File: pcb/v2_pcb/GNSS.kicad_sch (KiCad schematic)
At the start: 22 parts, among them J900 U.FL / Beitian BT-T076, U900 UM980

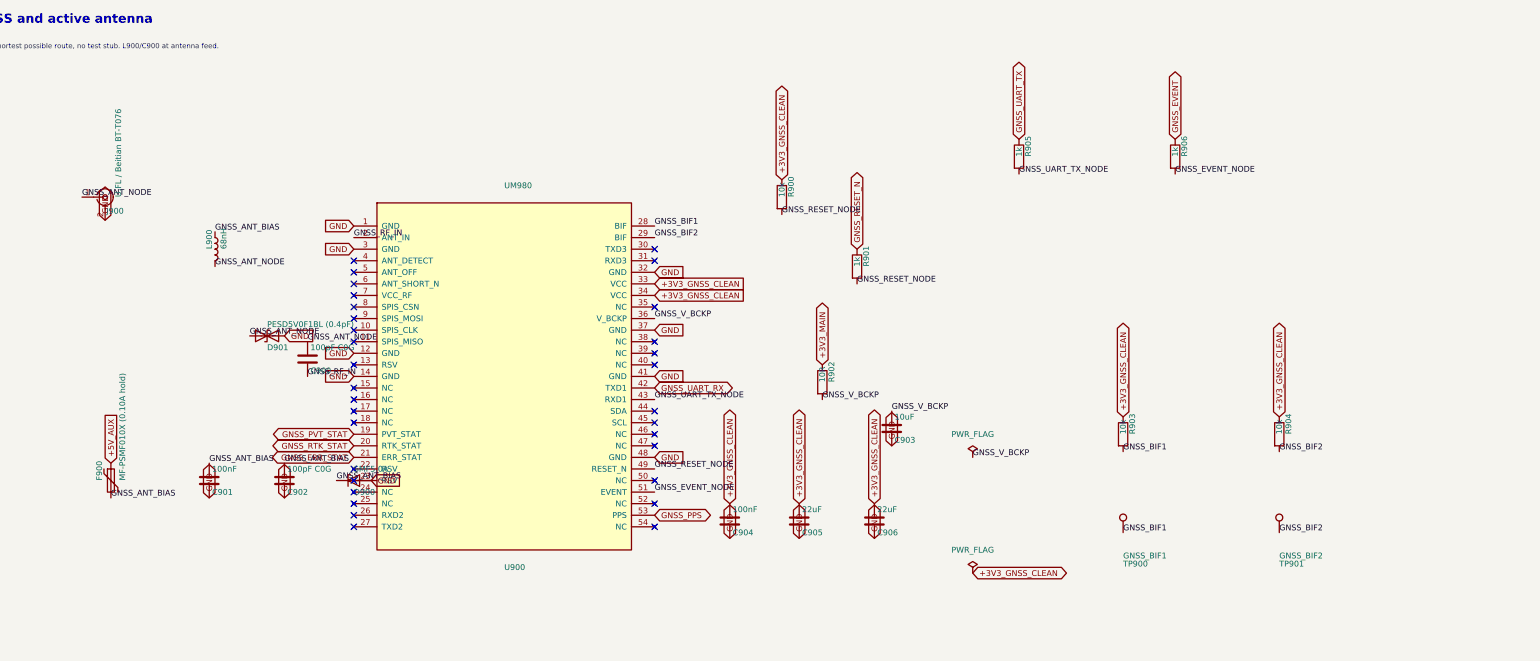
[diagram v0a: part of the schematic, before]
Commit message: switch mosfets
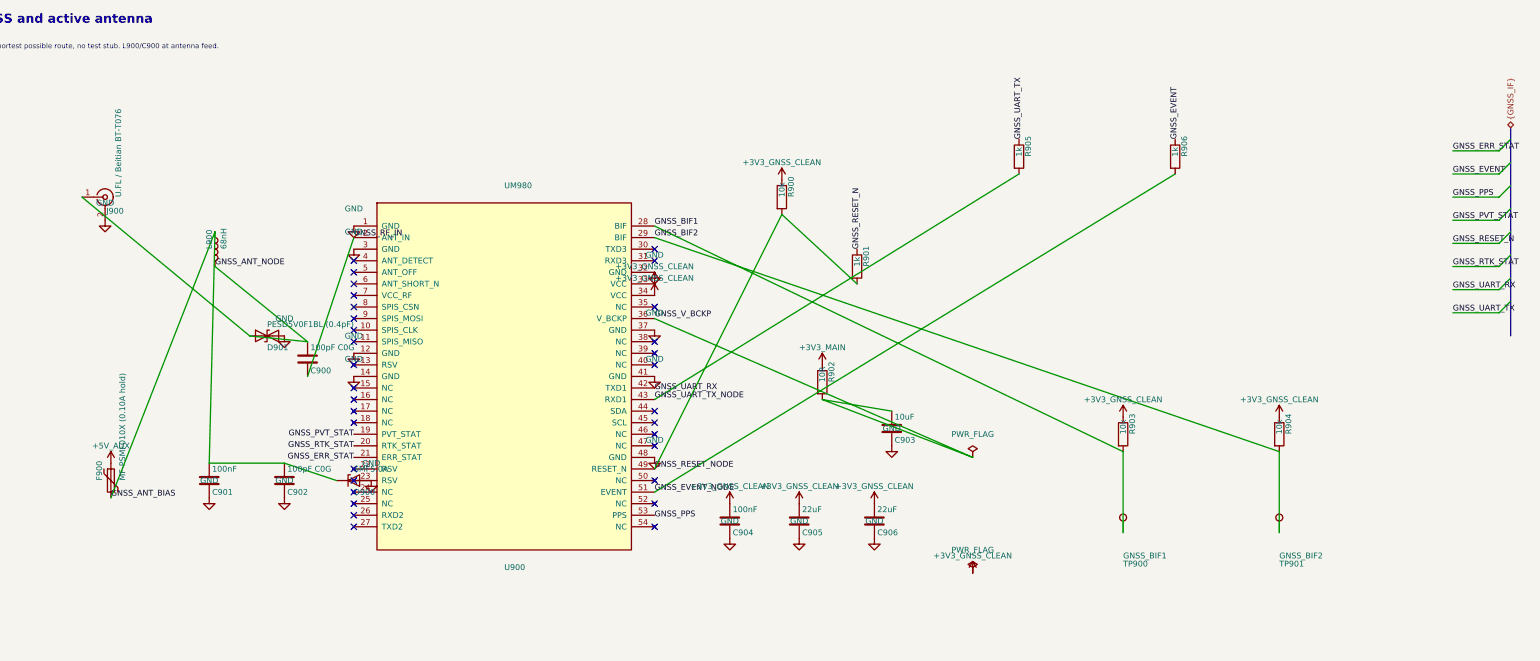
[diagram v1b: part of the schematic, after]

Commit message: clean debug and gnss
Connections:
- net GND: now also C900.2
- net GNSS_ANT_BIAS: no longer names the net of C901.1, C902.1, D900.1 (K), F900.2
- net GNSS_ANT_BIAS: now also L900.2; no longer L900.1
- net GNSS_ANT_NODE: no longer names the net of C900.1, D901.1 (A1), J900.1 (In)
- net GNSS_ANT_NODE: now also L900.1, U900.2 (ANT_IN); no longer L900.2
- net GNSS_BIF1: no longer names the net of R903.2, TP900.1, U900.28 (BIF)
- net GNSS_BIF2: no longer names the net of R904.2, TP901.1, U900.29 (BIF)
- net GNSS_EVENT_NODE: no longer names the net of R906.2, U900.51 (EVENT)
- net GNSS_RESET_NODE: no longer names the net of R900.2, R901.2, U900.49 (RESET_N)
- removed net GNSS_RF_IN: C900.2, U900.2 (ANT_IN)
- net GNSS_UART_TX_NODE: no longer names the net of R905.2, U900.43 (RXD1)
- net GNSS_V_BCKP: no longer names the net of C903.1, R902.2, U900.36 (V_BCKP)
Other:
- moved on the sheet: C900, C901, C902, C903, C904, C905, C906, D900, D901, F900, J900, L900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

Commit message: clean pcb
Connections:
- net GNSS_V_BCKP: now reaches C903.1, R902.2, U900.36 (V_BCKP)
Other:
- moved on the sheet: C900, C901, C902, C903, C904, C905, C906, D900, D901, F900, J900, L900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

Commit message: fix minor
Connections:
- net GND: now also D900.1 (K); no longer C900.2, D900.2 (A)
- net at C901.1, C902.1, F900.2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: now also D900.2 (A); no longer D900.1 (K)
- net at C900.1, D901.1 (A1), J900.1 (In)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: no longer U900.2 (ANT_IN)
- new net: C900.2, U900.2 (ANT_IN)
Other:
- moved on the sheet: C900, D900
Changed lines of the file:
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@@
 	(wire
 		(pts
-			(xy 162.56 104.14) (xy 171.45 104.14)
-		)
-		(stroke
-			(width 0)
-			(type default)
-		)
-	)
-	(wire
-		(pts
 			(xy 323.85 146.05) (xy 349.25 146.05)
 		)
@@
 	(wire
 		(pts
-			(xy 171.45 96.52) (xy 181.61 96.52)
+			(xy 179.07 96.52) (xy 181.61 96.52)
 		)
 		(stroke
@@
 	(symbol
 		(lib_id "Device:D_Zener")
-		(at 173.99 118.11 270)
+		(at 173.99 118.11 90)
 		(unit 1)
 		(body_style 1)
@@
 	(symbol
 		(lib_id "Device:C")
-		(at 171.45 100.33 0)
+		(at 175.26 96.52 90)
 		(unit 1)
 		(body_style 1)
@@
 		(dnp no)
 		(property "Reference" "C900"
-			(at 175.26 100.33 0)
+			(at 175.26 92.71 0)
 			(show_name no)
 			(do_not_autoplace no)
@@
 		)
 		(property "Value" "100pF C0G"
-			(at 177.8 101.6 0)
+			(at 175.26 91.44 0)
 			(show_name no)
 			(do_not_autoplace no)

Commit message: small
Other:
- moved on the sheet: R903, R904, TP900, TP901

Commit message: minor fixes
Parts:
- C900, C902: value 100pF C0G -> 100pF 50V C0G; Dielectric (none) -> C0G; MPN (none) -> CGA2B2C0G1H101J050BE; Manufacturer (none) -> TDK; Qualification (none) -> AEC-Q200; Tolerance (none) -> ±5%; Voltage (none) -> 50 VDC
- C901, C904: value 100nF -> 100nF 50V X7R; Dielectric (none) -> X7R; MPN (none) -> CGA2B3X7R1H104K050BE; Manufacturer (none) -> TDK; Qualification (none) -> AEC-Q200; Termination (none) -> Soft termination; Tolerance (none) -> ±10%; Voltage (none) -> 50 VDC
- C903: value 10uF -> 10uF 10V X7R; Dielectric (none) -> X7R; MPN (none) -> GCJ21BR71A106KE01L; Manufacturer (none) -> Murata; Qualification (none) -> AEC-Q200; Termination (none) -> Soft termination; Tolerance (none) -> ±10%; Voltage (none) -> 10 VDC
- C905, C906: value 22uF -> 22uF 6.3V X7T; Dielectric (none) -> X7T; MPN (none) -> GCJ21BD70J226ME02L; Manufacturer (none) -> Murata; Qualification (none) -> AEC-Q200; Release_Status (none) -> Verify effective capacitance under 3.3 V DC bias; Termination (none) -> Soft termination; Tolerance (none) -> ±20%; Voltage (none) -> 6.3 VDC
- D900: footprint Diode_SMD:D_SOD-123F -> open-race-v2:SOD-123FL_Littelfuse_SMF; Design_Note (none) -> Exact Littelfuse SOD-123FL land: 1.6 x 1.4 mm pads, 1.3 mm 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
- F900: value MF-PSMF010X (0.10A hold) -> MF-PSMF020X-2 (0.20A hold @23C); Design_Note (none) -> Sized above UM980 VCC_RF 50 mA limit; Ihold is 70 mA at 85 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; MPN MF-PSMF010X-2 -> MF-PSMF020X-2
- J900: value U.FL / Beitian BT-T076 -> U.FL-R-SMT-1(10); Design_Note (none) -> The selected BT-T076 antenna terminates in SMA-J. Add a con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; Manufacturer Hirose -> Hirose Electric; Notes (none) -> Board connector only; external antenna and pigtail belong i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
- L900: value 68nH -> LQW18AN68NG00D 68nH 2%; Design_Note (none) -> GNSS active-antenna bias RFC. Q>=38 at 200 MHz, SRF>=2.2 GH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; MPN (none) -> LQW18AN68NG00D; Manufacturer (none) -> Murata Electronics
- R900, R903, R904: MPN (none) -> CRCW040210K0FKED; Manufacturer (none) -> Vishay; Power (none) -> 0.063 W; TCR (none) -> ±100 ppm/K; Tolerance (none) -> ±1%
- R901, R905, R906: MPN (none) -> CRCW04021K00FKED; Manufacturer (none) -> Vishay; Power (none) -> 0.063 W; TCR (none) -> ±100 ppm/K; Tolerance (none) -> ±1%
- R902: MPN (none) -> CRCW040210R0FKED; Manufacturer (none) -> Vishay; Power (none) -> 0.063 W; TCR (none) -> ±100 ppm/K; Tolerance (none) -> ±1%
- TP900, TP901: now left out of the parts list
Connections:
- net GND: now also D900.2 (A); no longer D900.1 (K)
- net at C901.1, C902.1, F900.2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: now also D900.1 (K); no longer D900.2 (A)
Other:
- note added: "ANTENNA ASSEMBLY HOLD: BT-T076 is SMA-J while J900 is U.FL. Specify a controlled pigtail; verify 3.3-5.0 V at the antenna over rail/cable tolerance, <=55 mA, and -40 to +70 C."
- moved on the sheet: D900
